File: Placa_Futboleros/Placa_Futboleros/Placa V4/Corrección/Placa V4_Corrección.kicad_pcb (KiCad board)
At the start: 2 copper layers, 100 x 70 mm, 31 parts, among them J1 LiPo, J2 MI_Ad, J3 MI_At, J4 MD_Ad, J5 MD_At, J6 Pilas, U1 ESP32_30p, U2 DRV8833, U3 DRV8833, U5 INA219AxD

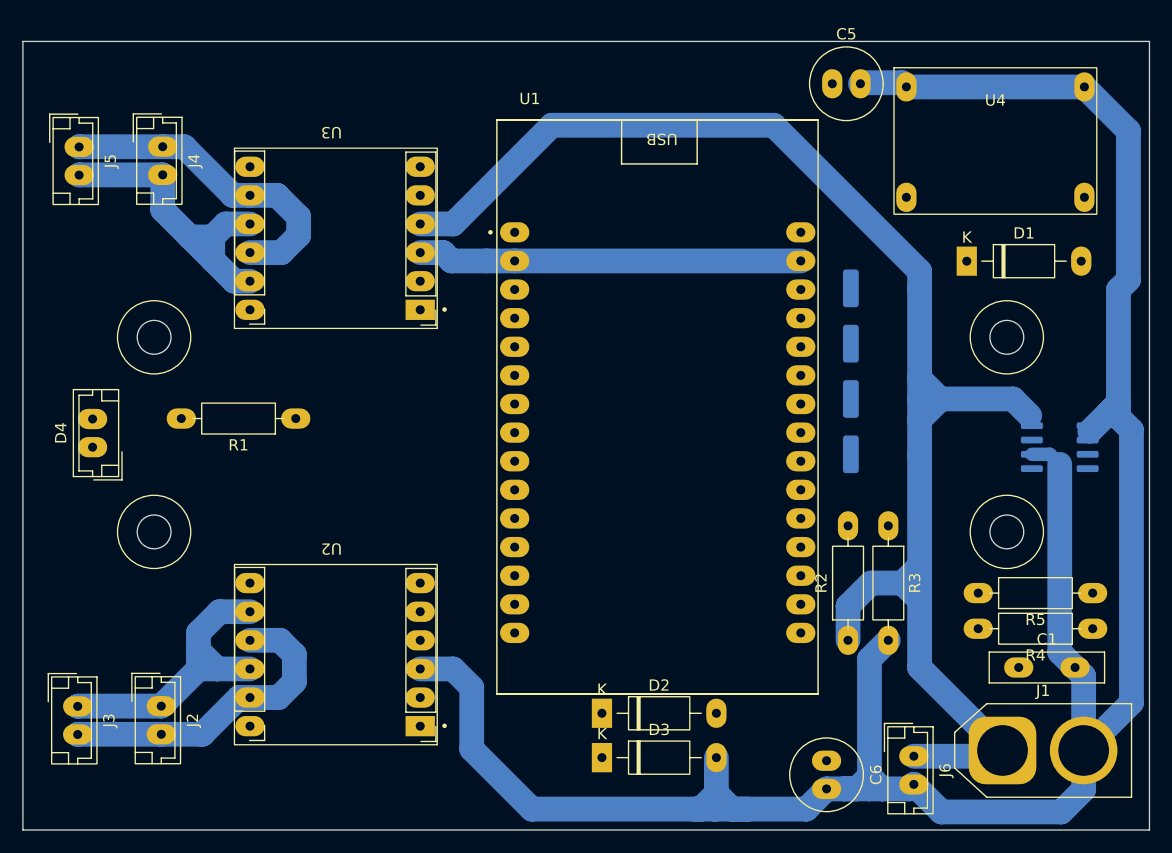
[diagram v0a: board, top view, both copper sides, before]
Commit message: Pusheo de archivos varios del SementalItaliano
1. Diseños de solid edge del robot:
  - Se utiliza ahora únicamente dos motores más potentes.
  - Eso requiere un sistema de engranajes, donde los ejes de las ruedas de atrás
  son del motor, hay engranajes bobos en medio y luego las ruedas delanteras.
  - Se agrega la llave en la tapa para ON-OFF del robot.
  - La LiPo es más grande.

2. Cambio de LiPo a una de 14,8V 2200mAh con 45C.
3. Se rehace por ese motivo la placa, con drivers BTS7960, así que se redistribuye cosas
en el robot, y se agrega para montar y desmontar el módulo de la placa.
4. Las placas tiene 1,7mm de ancho de pista grande y 0,8 creo de pistas chicas; hay solo dos puentes,
uno chiquito y otro corto pero de cable grueso, se adaptó el orificio para que pase bien el cable.
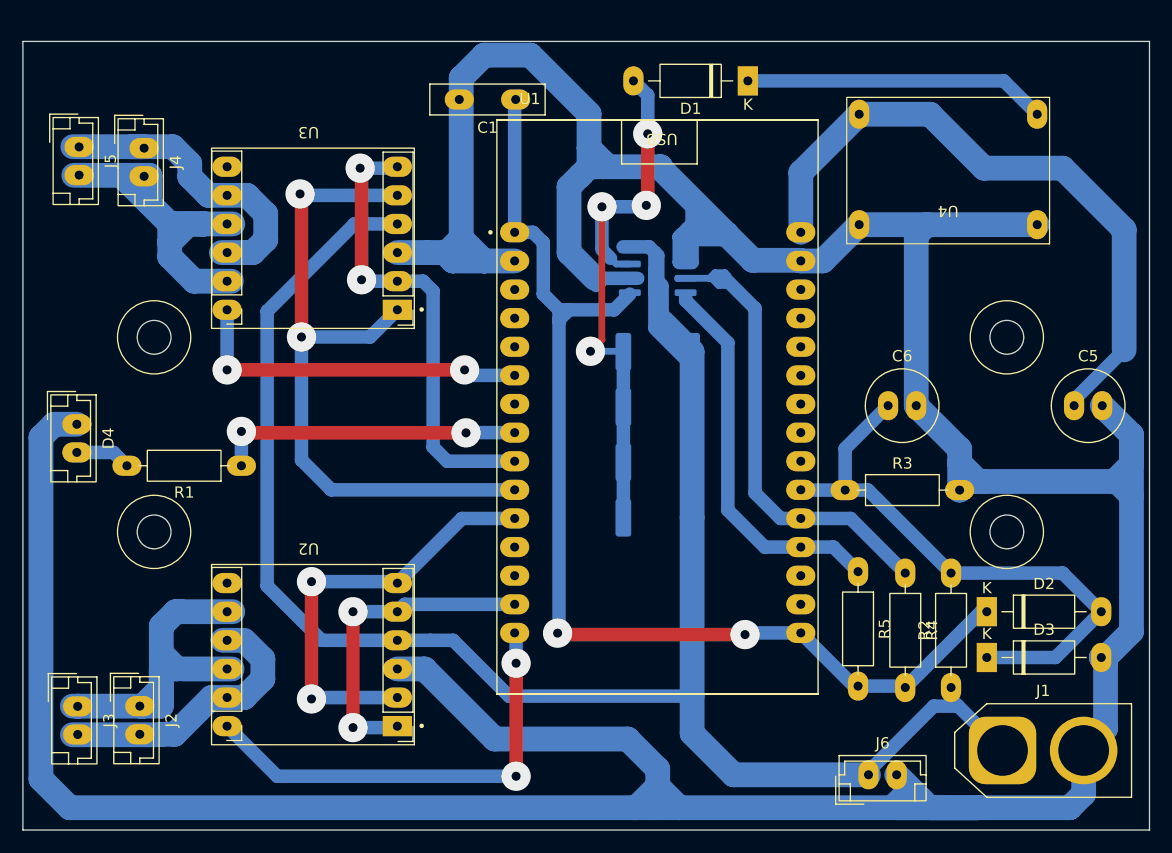
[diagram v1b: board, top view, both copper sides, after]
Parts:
- moved C1 67.4 mm to (84.5, 32.2), turned to 180 degrees
- moved U5 39.0 mm to (97.1, 47.4)
- moved C5 35.7 mm to (134.0, 59.4)
- moved D2 35.3 mm to (126.3, 77.7)
- moved D3 35.3 mm to (126.3, 81.7)
- moved C6 32.0 mm to (117.5, 59.4), turned to 0 degrees
- moved D1 25.2 mm to (105.1, 30.6), turned to 180 degrees
- moved R10 21.0 mm to (97.1, 69.3)
- moved R7 21.0 mm to (97.1, 54.6)
- moved R8 21.0 mm to (97.1, 59.5)
- moved R9 21.0 mm to (97.1, 64.4)
- moved R5 20.9 mm to (114.8, 74.1), turned to -90 degrees
- moved R4 17.4 mm to (119.0, 74.2), turned to -90 degrees
- moved R2 10.1 mm to (123.1, 84.4)
- moved R1 6.39 mm to (60.1, 64.7)
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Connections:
- U1 pad 11: unconnected-(U1-D21-Pad11) -> IN_M1B
- U1 pad 14: unconnected-(U1-D22-Pad14) -> IN_M1A
- U1 pad 15: SLEEP_M2 -> SLEEP_M1
- U1 pad 23: IN_M1A -> unconnected-(U1-D25-Pad23)
- U1 pad 24: IN_M1B -> unconnected-(U1-D26-Pad24)
- U1 pad 6: SLEEP_M1 -> SLEEP_M2
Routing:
- net GND: track 253.2 -> 401.1 mm
- net 3V3: track 0.00 -> 101.4 mm, vias 0 -> 2
- net IN_M2A: track 0.00 -> 61.9 mm, vias 0 -> 2
- net Net-(D1-A): track 0.00 -> 60.3 mm, vias 0 -> 4
- net 5V: track 0.00 -> 57.9 mm
- net /ADC: track 0.00 -> 52.1 mm
- net SDA: track 0.00 -> 44.0 mm
- net IN_M2B: track 0.00 -> 41.7 mm, vias 0 -> 2
- net SLEEP_M1: track 0.00 -> 40.3 mm, vias 0 -> 2
- net IN_M1B: track 0.00 -> 38.5 mm, vias 0 -> 2
- net VCC: track 139.8 -> 177.8 mm
- net SCL: track 0.00 -> 34.3 mm
- net SLEEP_M2: track 0.00 -> 31.1 mm, vias 0 -> 2
- net IN_M1A: track 0.00 -> 28.9 mm, vias 0 -> 2
- net LED_Encendido: track 0.00 -> 27.4 mm, vias 0 -> 2
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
